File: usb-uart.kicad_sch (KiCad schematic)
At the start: 9 parts

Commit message: v2 time
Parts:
- gave numbers to parts that had none: 5
- renumbered R18 to R16, TP17 to TP7, TP18 to TP8, TP19 to TP9
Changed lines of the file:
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@@
   (symbol (lib_id "power:GND") (at 127 96.52 90) (unit 1)
     (in_bom yes) (on_board yes)
-    (property "Reference" "#PWR?" (id 0) (at 133.35 96.52 0)
+    (property "Reference" "#PWR038" (id 0) (at 133.35 96.52 0)
       (effects (font (size 1.27 1.27)) hide)
     )
@@
   (symbol (lib_id "Device:R_Small") (at 123.19 99.06 270) (unit 1)
     (in_bom yes) (on_board yes)
-    (property "Reference" "R?" (id 0) (at 129.54 100.33 90))
+    (property "Reference" "R15" (id 0) (at 129.54 100.33 90))
     (property "Value" "5.1k" (id 1) (at 129.54 102.6414 90))
     (property "Footprint" "Resistor_SMD:R_0402_1005Metric" (id 2) (at 123.19 99.06 0)
@@
   (symbol (lib_id "Device:R_Small") (at 123.19 93.98 90) (unit 1)
     (in_bom yes) (on_board yes)
-    (property "Reference" "R?" (id 0) (at 123.19 89.0016 90))
+    (property "Reference" "R14" (id 0) (at 123.19 89.0016 90))
     (property "Value" "5.1k" (id 1) (at 123.19 91.313 90))
     (property "Footprint" "Resistor_SMD:R_0402_1005Metric" (id 2) (at 123.19 93.98 0)
@@
   (symbol (lib_id "power:GND") (at 96.52 130.81 0) (unit 1)
     (in_bom yes) (on_board yes)
-    (property "Reference" "#PWR?" (id 0) (at 96.52 137.16 0)
+    (property "Reference" "#PWR036" (id 0) (at 96.52 137.16 0)
       (effects (font (size 1.27 1.27)) hide)
     )
@@
   (symbol (lib_id "Connector:USB_C_Receptacle_USB2.0") (at 100.33 104.14 0) (unit 1)
     (in_bom yes) (on_board yes)
-    (property "Reference" "J?" (id 0) (at 103.0478 82.1182 0))
+    (property "Reference" "J5" (id 0) (at 103.0478 82.1182 0))
     (property "Value" "USB_C_Receptacle_USB2.0" (id 1) (at 103.0478 84.4296 0))
     (property "Footprint" "Connector_USB:USB_C_Receptacle_GCT_USB4085" (id 2) (at 104.14 104.14 0)
@@
   (symbol (lib_id "power:GND") (at 132.08 144.78 0) (unit 1)
     (in_bom yes) (on_board yes)
-    (property "Reference" "#PWR?" (id 0) (at 132.08 151.13 0)
+    (property "Reference" "#PWR039" (id 0) (at 132.08 151.13 0)
       (effects (font (size 1.27 1.27)) hide)
     )
@@
   (symbol (lib_id "Power_Protection:SP0503BAHT") (at 132.08 139.7 0) (unit 1)
     (in_bom yes) (on_board yes)
-    (property "Reference" "D?" (id 0) (at 137.287 138.5316 0)
+    (property "Reference" "D6" (id 0) (at 137.287 138.5316 0)
       (effects (font (size 1.27 1.27)) (justify left))
     )
@@
   (symbol (lib_id "power:VBUS") (at 116.84 85.09 0) (unit 1)
     (in_bom yes) (on_board yes)
-    (property "Reference" "#PWR?" (id 0) (at 116.84 88.9 0)
+    (property "Reference" "#PWR037" (id 0) (at 116.84 88.9 0)
       (effects (font (size 1.27 1.27)) hide)
     )
@@
   (symbol (lib_id "Connector:TestPoint") (at 52.07 99.06 270) (unit 1)
     (in_bom yes) (on_board yes)
-    (property "Reference" "TP?" (id 0) (at 56.8452 97.8916 90)
+    (property "Reference" "TP7" (id 0) (at 56.8452 97.8916 90)
       (effects (font (size 1.27 1.27)) (justify left))
     )
@@
   (symbol (lib_id "Connector:TestPoint") (at 52.07 104.14 270) (unit 1)
     (in_bom yes) (on_board yes)
-    (property "Reference" "TP?" (id 0) (at 56.8452 102.9716 90)
+    (property "Reference" "TP8" (id 0) (at 56.8452 102.9716 90)
       (effects (font (size 1.27 1.27)) (justify left))
     )
@@
   (symbol (lib_id "Connector:TestPoint") (at 52.07 109.22 270) (unit 1)
     (in_bom yes) (on_board yes)
-    (property "Reference" "TP?" (id 0) (at 56.8452 108.0516 90)
+    (property "Reference" "TP9" (id 0) (at 56.8452 108.0516 90)
       (effects (font (size 1.27 1.27)) (justify left))
     )
@@
   (symbol (lib_id "Device:LED_Small") (at 162.56 92.71 180) (unit 1)
     (in_bom yes) (on_board yes)
-    (property "Reference" "USBLED?" (id 0) (at 162.56 87.503 0))
+    (property "Reference" "USBLED1" (id 0) (at 162.56 87.503 0))
     (property "Value" "USB_LED" (id 1) (at 162.56 89.8144 0))
     (property "Footprint" "Resistor_SMD:R_0402_1005Metric" (id 2) (at 162.56 92.71 90)
@@
   (symbol (lib_id "Device:R_Small") (at 154.94 92.71 90) (unit 1)
     (in_bom yes) (on_board yes)
-    (property "Reference" "R?" (id 0) (at 154.94 97.6884 90))
+    (property "Reference" "R16" (id 0) (at 154.94 97.6884 90))
     (property "Value" "470" (id 1) (at 154.94 95.377 90))
     (property "Footprint" "Resistor_SMD:R_0402_1005Metric" (id 2) (at 154.94 92.71 0)
@@
   (symbol (lib_id "power:GND") (at 165.1 92.71 90) (unit 1)
     (in_bom yes) (on_board yes)
-    (property "Reference" "#PWR?" (id 0) (at 171.45 92.71 0)
+    (property "Reference" "#PWR041" (id 0) (at 171.45 92.71 0)
       (effects (font (size 1.27 1.27)) hide)
     )
@@
   (symbol (lib_id "power:VBUS") (at 152.4 92.71 90) (unit 1)
     (in_bom yes) (on_board yes)
-    (property "Reference" "#PWR?" (id 0) (at 156.21 92.71 0)
-      (effects (font (size 1.27 1.27)) hide)
-    )
+    (property "Reference" "#PWR040" (id 0) (at 156.21 92.71 0)
+      (effects (font (size 1.27 1.27)) hide)
+    )

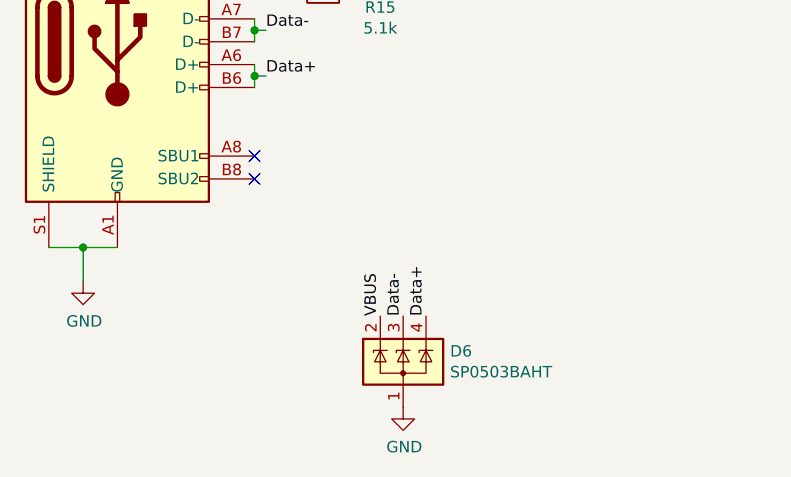
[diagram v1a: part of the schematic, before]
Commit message: Conitnued with v2, NB pinout of external sd card has changed!!! Chest needs to be updated before manufacturing!!!
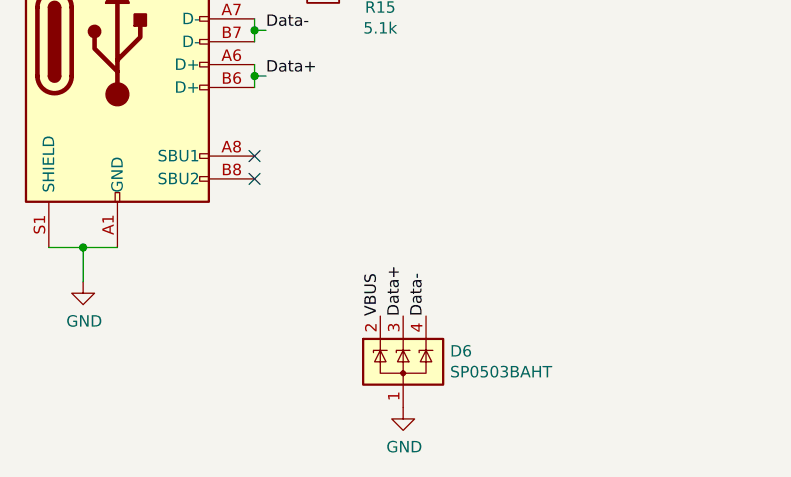
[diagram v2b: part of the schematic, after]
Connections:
- net Data+: now also D6.3 (K); no longer D6.4 (K)
- net Data-: now also D6.4 (K); no longer D6.3 (K)
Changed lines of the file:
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@@
     (stroke (width 0) (type default) (color 0 0 0 0))
   )
-  (label "Data+" (at 134.62 134.62 90)
+  (label "Data+" (at 132.08 134.62 90)
     (effects (font (size 1.27 1.27)) (justify left bottom))
   )
@@
     (effects (font (size 1.27 1.27)) (justify left bottom))
   )
-  (label "Data-" (at 132.08 134.62 90)
+  (label "Data-" (at 134.62 134.62 90)
     (effects (font (size 1.27 1.27)) (justify left bottom))
   )

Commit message: made more progress
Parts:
- J5: footprint Connector_USB:USB_C_Receptacle_GCT_USB4085 -> Connector_USB:USB_C_Receptacle_Palconn_UTC16-G
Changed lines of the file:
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@@
     (property "Reference" "J5" (id 0) (at 103.0478 82.1182 0))
     (property "Value" "USB_C_Receptacle_USB2.0" (id 1) (at 103.0478 84.4296 0))
-    (property "Footprint" "Connector_USB:USB_C_Receptacle_GCT_USB4085" (id 2) (at 104.14 104.14 0)
+    (property "Footprint" "Connector_USB:USB_C_Receptacle_Palconn_UTC16-G" (id 2) (at 104.14 104.14 0)
       (effects (font (size 1.27 1.27)) hide)
     )

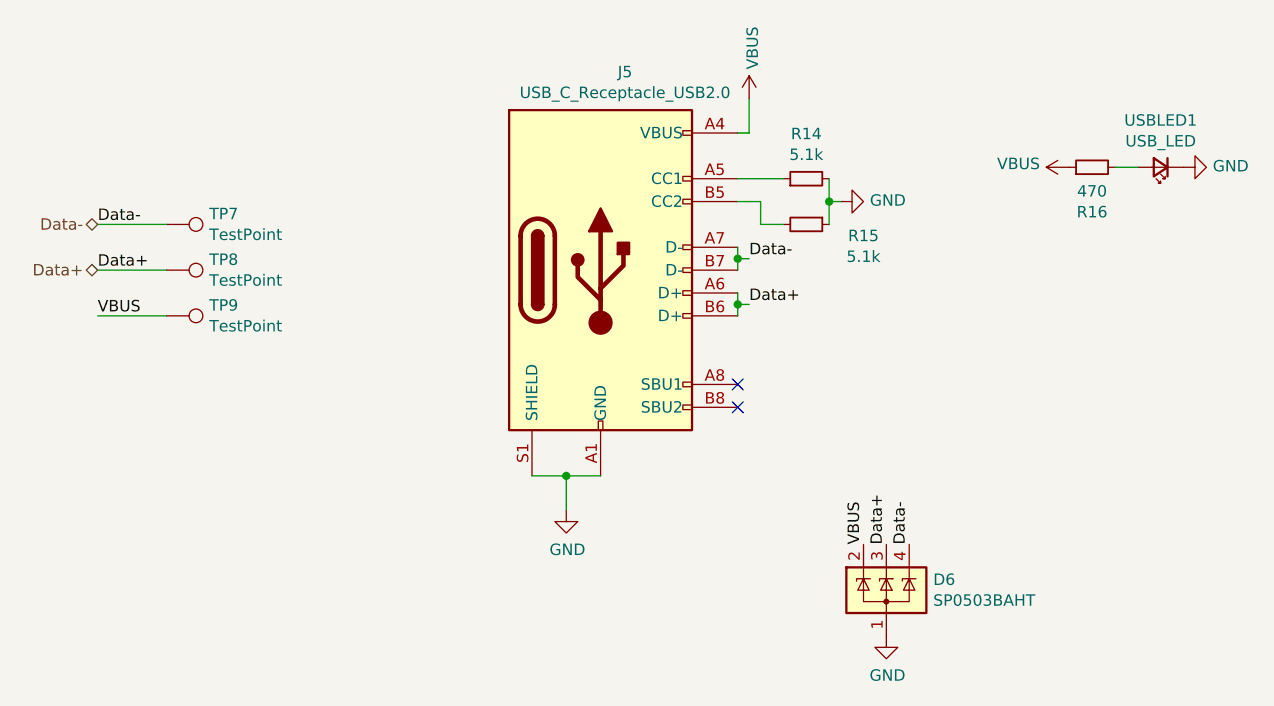
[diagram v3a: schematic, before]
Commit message: changed bb and power side
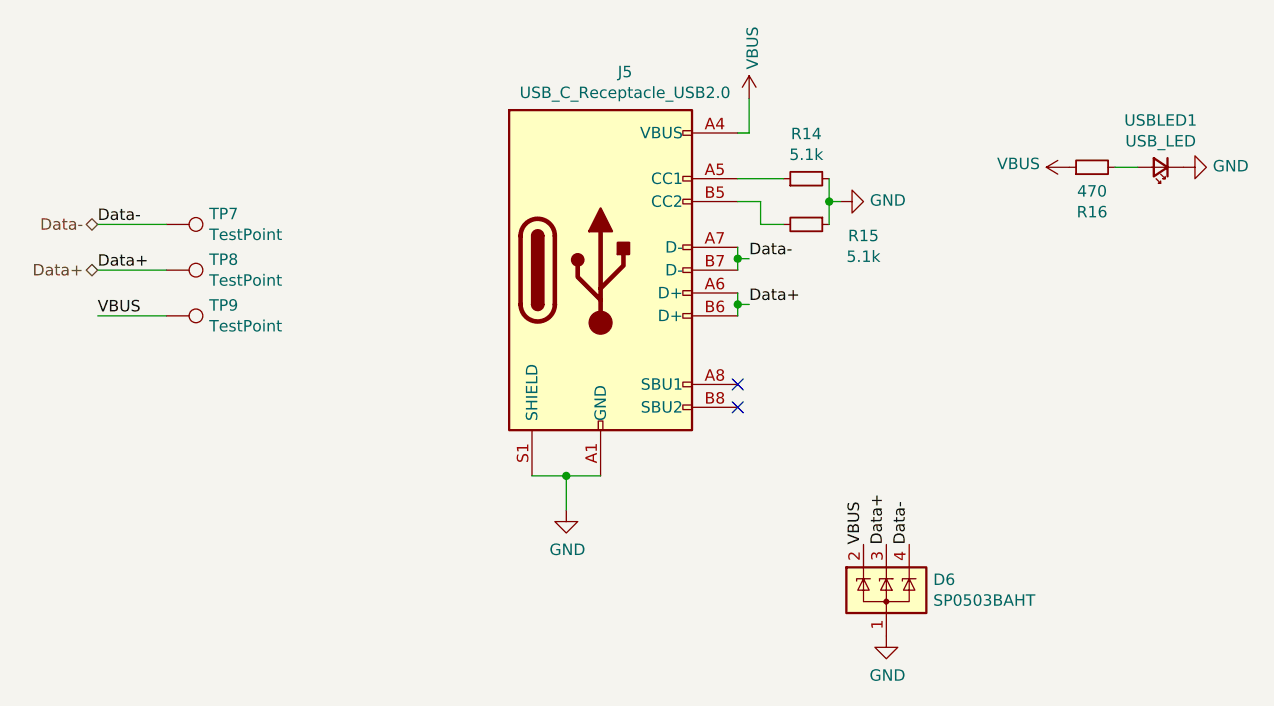
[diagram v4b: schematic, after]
